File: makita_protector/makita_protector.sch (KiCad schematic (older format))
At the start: 42 parts, among them J1 Jack-DC, Q1 SQJ457EP, Q2 BSS123, SW1 FORCE_ON, SW2 FORCE_OFF, U1 TPS54302, U2 LM2903

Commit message: first layout
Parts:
- removed C1, C12: 100n, symbol Device:C
- removed C2, C4, C7, C9: 10u, symbol Device:C
- removed C6: 100p, symbol Device:C
- removed J1: Jack-DC, symbol Connector:Jack-DC
- removed L1: INDUCTOR, symbol pspice:INDUCTOR
- removed R1, R2: R, symbol Device:R
- removed R5: 47R, symbol Device:R
- removed R6: 100k, symbol Device:R
- removed R7: 5k6, symbol Device:R
- removed SW1: FORCE_ON, symbol Switch:SW_Push
- removed SW2: FORCE_OFF, symbol Switch:SW_Push
- removed U1: TPS54302, Package_TO_SOT_SMD:SOT-23-6, symbol Regulator_Switching:TPS54302
- added F2: Fuse, Fuse:Fuse_0603_1608Metric, symbol Device:Fuse
- added H? (x4): MountingHole, symbol Mechanical:MountingHole
- added J1: 12V, TestPoint:TestPoint_Plated_Hole_D2.0mm, symbol Connector_Generic:Conn_01x01
- added J2, J4, J6: GND, TestPoint:TestPoint_Plated_Hole_D2.0mm, symbol Connector_Generic:Conn_01x01
- added J3: FORCE_ON, TestPoint:TestPoint_Plated_Hole_D2.0mm, symbol Connector_Generic:Conn_01x01
- added J5: FORCE_OFF, TestPoint:TestPoint_Plated_Hole_D2.0mm, symbol Connector_Generic:Conn_01x01
- BT1: footprint (none) -> makita_protector:contact_plates
- C10, C3, C5, C8: footprint (none) -> Capacitor_SMD:C_0805_2012Metric
- C13: renamed from C11; footprint (none) -> Capacitor_SMD:C_0805_2012Metric
- F1: footprint (none) -> Fuse:Fuse_1206_3216Metric
- R10: renamed from R12; footprint (none) -> Resistor_SMD:R_0805_2012Metric
- R13: renamed from R10; footprint (none) -> Resistor_SMD:R_0805_2012Metric
- R14: renamed from R11; footprint (none) -> Resistor_SMD:R_0805_2012Metric
- R15: renamed from R13; footprint (none) -> Resistor_SMD:R_0805_2012Metric
- R16: renamed from R14; footprint (none) -> Resistor_SMD:R_0805_2012Metric
- R20: renamed from R15; footprint (none) -> Resistor_SMD:R_0805_2012Metric
- R21: renamed from R16; footprint (none) -> Resistor_SMD:R_0805_2012Metric
- R3, R4, R8, R9: footprint (none) -> Resistor_SMD:R_0805_2012Metric
- U2: footprint (none) -> Package_SO:SOIC-8_3.9x4.9mm_P1.27mm
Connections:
- net +12V: now also J1.1 (Pin_1)
- net +BATT: now also F2.1
- net GND: now also J2.1 (Pin_1), J4.1 (Pin_1), J6.1 (Pin_1)
- net at BT1.1 (+), F1.2: now also F2.2
- net at C3.2: now also J3.1 (Pin_1)
- net at R16.2: now also J5.1 (Pin_1)
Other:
- note removed: "DCDC"
- note removed: "EN pin maximum 6V!"
- note removed: "battery voltage to output voltage"
- moved on the sheet: BT1, C10, C13, C3, C5, C8, D1, D2, D3, D4, F1, Q1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

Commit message: updated layput
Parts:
- H1, H2, H3, H4: renamed from H?; footprint (none) -> MountingHole:MountingHole_3.2mm_M3_DIN965
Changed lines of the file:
@@
 F 0 "#LOGO1" H 6000 7375 50  0001 C CNN
 F 1 "Logo_Open_Hardware_Small" H 6000 6875 50  0001 C CNN
-F 2 "" H 6000 7100 50  0001 C CNN
+F 2 "Symbol:OSHW-Logo2_9.8x8mm_Copper" H 6000 7100 50  0001 C CNN
 F 3 "~" H 6000 7100 50  0001 C CNN
 	1    6000 7100
@@
 	9600 1950 9600 2700
 $Comp
-L Mechanical:MountingHole H?
+L Mechanical:MountingHole H1
 U 1 1 6025B2E9
 P 1000 6400
-F 0 "H?" H 1100 6446 50  0000 L CNN
+F 0 "H1" H 1100 6446 50  0000 L CNN
 F 1 "MountingHole" H 1100 6355 50  0000 L CNN
-F 2 "" H 1000 6400 50  0001 C CNN
+F 2 "MountingHole:MountingHole_3.2mm_M3_DIN965" H 1000 6400 50  0001 C CNN
 F 3 "~" H 1000 6400 50  0001 C CNN
 	1    1000 6400
@@
 $EndComp
 $Comp
-L Mechanical:MountingHole H?
+L Mechanical:MountingHole H2
 U 1 1 6025BA60
 P 1000 6600
-F 0 "H?" H 1100 6646 50  0000 L CNN
+F 0 "H2" H 1100 6646 50  0000 L CNN
 F 1 "MountingHole" H 1100 6555 50  0000 L CNN
-F 2 "" H 1000 6600 50  0001 C CNN
+F 2 "MountingHole:MountingHole_3.2mm_M3_DIN965" H 1000 6600 50  0001 C CNN
 F 3 "~" H 1000 6600 50  0001 C CNN
 	1    1000 6600
@@
 $EndComp
 $Comp
-L Mechanical:MountingHole H?
+L Mechanical:MountingHole H3
 U 1 1 6025C1C4
 P 1000 6800
-F 0 "H?" H 1100 6846 50  0000 L CNN
+F 0 "H3" H 1100 6846 50  0000 L CNN
 F 1 "MountingHole" H 1100 6755 50  0000 L CNN
-F 2 "" H 1000 6800 50  0001 C CNN
+F 2 "MountingHole:MountingHole_3.2mm_M3_DIN965" H 1000 6800 50  0001 C CNN
 F 3 "~" H 1000 6800 50  0001 C CNN
 	1    1000 6800
@@
 $EndComp
 $Comp
-L Mechanical:MountingHole H?
+L Mechanical:MountingHole H4
 U 1 1 6025C1CA
 P 1000 7000
-F 0 "H?" H 1100 7046 50  0000 L CNN
+F 0 "H4" H 1100 7046 50  0000 L CNN
 F 1 "MountingHole" H 1100 6955 50  0000 L CNN
-F 2 "" H 1000 7000 50  0001 C CNN
+F 2 "MountingHole:MountingHole_3.2mm_M3_DIN965" H 1000 7000 50  0001 C CNN
 F 3 "~" H 1000 7000 50  0001 C CNN
 	1    1000 7000
 	1    0    0    -1
 $EndComp
+$Comp
+L Graphic:Logo_Open_Hardware_Small #LOGO2
+U 1 1 6004B459
+P 4950 7100
+F 0 "#LOGO2" H 4950 7375 50  0001 C CNN
+F 1 "Kicad" H 4950 6875 50  0000 C CNN
+F 2 "Symbol:KiCad-Logo2_8mm_Copper" H 4950 7100 50  0001 C CNN
+F 3 "~" H 4950 7100 50  0001 C CNN
+	1    4950 7100
+	1    0    0    -1
+$EndComp

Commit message: final version for production v1
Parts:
- added FID1, FID2, FID3: Fiducial, makita_protector:Fiducial_1mm_Mask2mm_Paste, symbol Mechanical:Fiducial
- added LOGO1: oshw, Symbol:OSHW-Logo2_7.3x6mm_SilkScreen, symbol Graphic:Logo_Open_Hardware_Small
- added LOGO2: Kicad, Symbol:KiCad-Logo2_5mm_SilkScreen, symbol Graphic:Logo_Open_Hardware_Small
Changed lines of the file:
@@
 Connection ~ 1500 1400
 $Comp
-L Graphic:Logo_Open_Hardware_Small #LOGO1
+L Graphic:Logo_Open_Hardware_Small LOGO1
 U 1 1 6012B83E
 P 6000 7100
-F 0 "#LOGO1" H 6000 7375 50  0001 C CNN
-F 1 "Logo_Open_Hardware_Small" H 6000 6875 50  0001 C CNN
-F 2 "Symbol:OSHW-Logo2_9.8x8mm_Copper" H 6000 7100 50  0001 C CNN
+F 0 "LOGO1" H 6000 7375 50  0001 C CNN
+F 1 "oshw" H 6000 6875 50  0000 C CNN
+F 2 "Symbol:OSHW-Logo2_7.3x6mm_SilkScreen" H 6000 7100 50  0001 C CNN
 F 3 "~" H 6000 7100 50  0001 C CNN
 	1    6000 7100
@@
 $EndComp
 $Comp
-L Graphic:Logo_Open_Hardware_Small #LOGO2
+L Graphic:Logo_Open_Hardware_Small LOGO2
 U 1 1 6004B459
 P 4950 7100
-F 0 "#LOGO2" H 4950 7375 50  0001 C CNN
+F 0 "LOGO2" H 4950 7375 50  0001 C CNN
 F 1 "Kicad" H 4950 6875 50  0000 C CNN
-F 2 "Symbol:KiCad-Logo2_8mm_Copper" H 4950 7100 50  0001 C CNN
+F 2 "Symbol:KiCad-Logo2_5mm_SilkScreen" H 4950 7100 50  0001 C CNN
 F 3 "~" H 4950 7100 50  0001 C CNN
 	1    4950 7100
 	1    0    0    -1
 $EndComp
+$Comp
+L Mechanical:Fiducial FID1
+U 1 1 60086B21
+P 2350 6400
+F 0 "FID1" H 2435 6446 50  0000 L CNN
+F 1 "Fiducial" H 2435 6355 50  0000 L CNN
+F 2 "makita_protector:Fiducial_1mm_Mask2mm_Paste" H 2350 6400 50  0001 C CNN
+F 3 "~" H 2350 6400 50  0001 C CNN
+	1    2350 6400
+	1    0    0    -1
+$EndComp
+$Comp
+L Mechanical:Fiducial FID2
+U 1 1 60087198
+P 2350 6650
+F 0 "FID2" H 2435 6696 50  0000 L CNN
+F 1 "Fiducial" H 2435 6605 50  0000 L CNN
+F 2 "makita_protector:Fiducial_1mm_Mask2mm_Paste" H 2350 6650 50  0001 C CNN
+F 3 "~" H 2350 6650 50  0001 C CNN
+	1    2350 6650
+	1    0    0    -1
+$EndComp
+$Comp
+L Mechanical:Fiducial FID3
+U 1 1 60087324
+P 2350 6900
+F 0 "FID3" H 2435 6946 50  0000 L CNN
+F 1 "Fiducial" H 2435 6855 50  0000 L CNN
+F 2 "makita_protector:Fiducial_1mm_Mask2mm_Paste" H 2350 6900 50  0001 C CNN
+F 3 "~" H 2350 6900 50  0001 C CNN
+	1    2350 6900
+	1    0    0    -1
+$EndComp

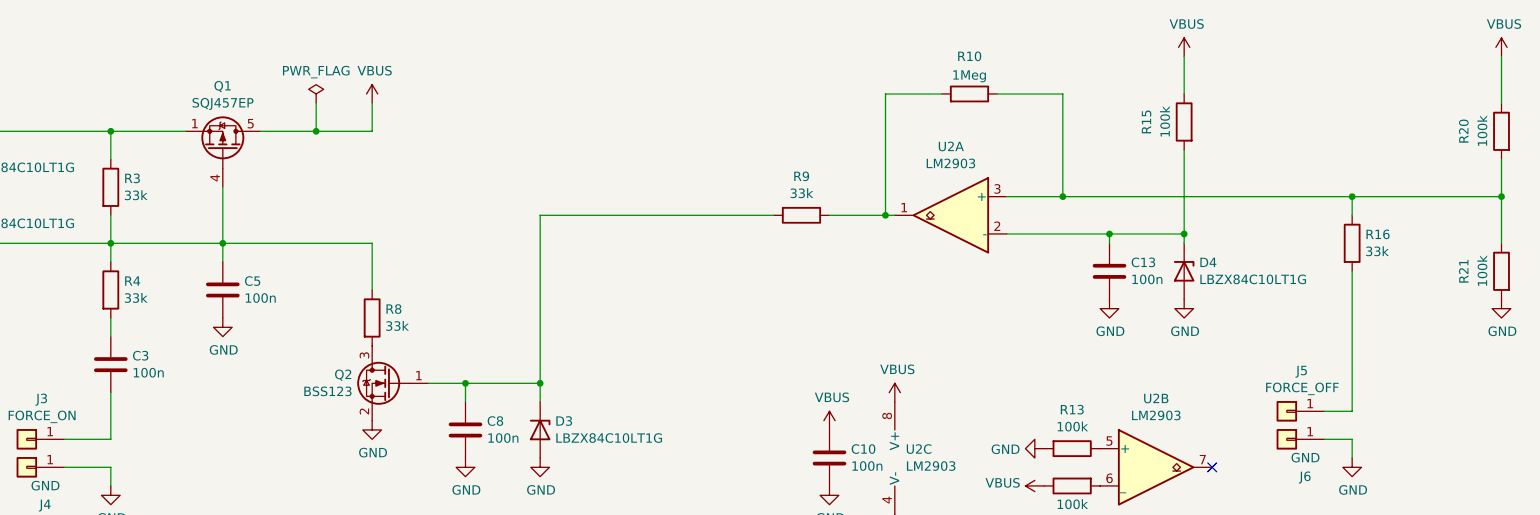
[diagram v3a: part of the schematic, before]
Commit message: updated values after initial testing
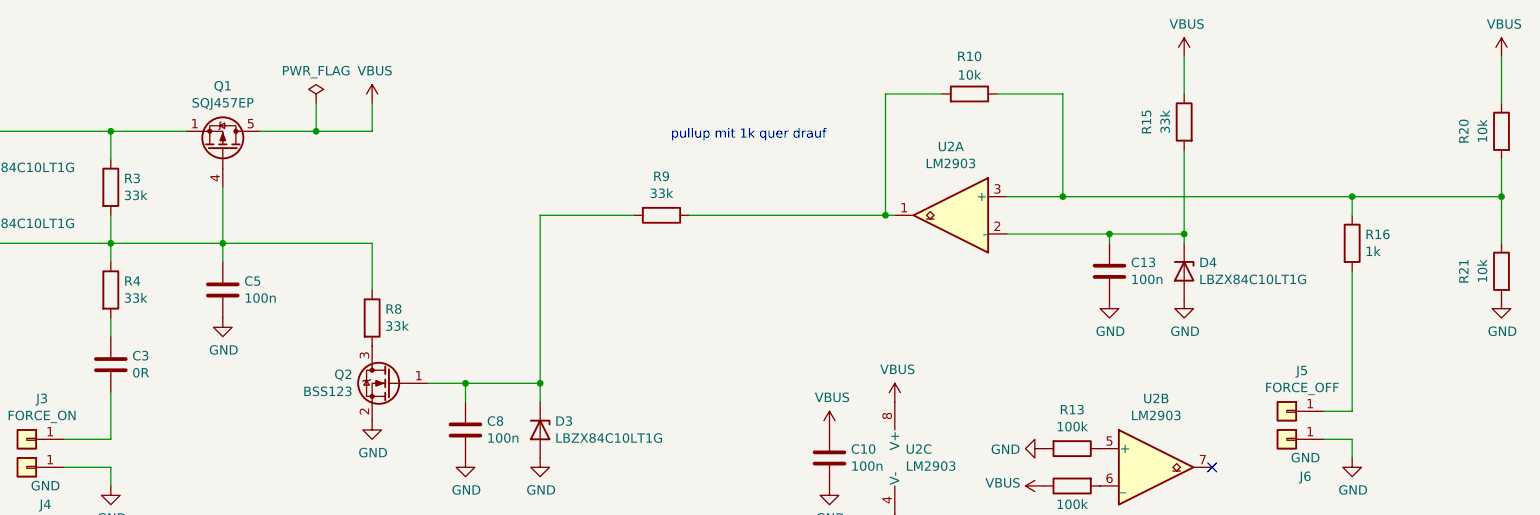
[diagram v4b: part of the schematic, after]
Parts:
- C3: value 100n -> 0R
- R10: value 1Meg -> 10k
- R15: value 100k -> 33k
- R16: value 33k -> 1k
- R20, R21: value 100k -> 10k
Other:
- note added: "pullup mit 1k quer drauf"
- moved on the sheet: R9
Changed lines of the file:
@@
 L Device:R R9
 U 1 1 6001C131
-P 6650 1650
-F 0 "R9" V 6443 1650 50  0000 C CNN
-F 1 "33k" V 6534 1650 50  0000 C CNN
-F 2 "Resistor_SMD:R_0805_2012Metric" V 6580 1650 50  0001 C CNN
-F 3 "~" H 6650 1650 50  0001 C CNN
-	1    6650 1650
+P 5900 1650
+F 0 "R9" V 5693 1650 50  0000 C CNN
+F 1 "33k" V 5784 1650 50  0000 C CNN
+F 2 "Resistor_SMD:R_0805_2012Metric" V 5830 1650 50  0001 C CNN
+F 3 "~" H 5900 1650 50  0001 C CNN
+	1    5900 1650
 	0    1    1    0
 $EndComp
@@
 P 8700 1150
 F 0 "R15" V 8900 1150 50  0000 C CNN
-F 1 "100k" V 8800 1150 50  0000 C CNN
+F 1 "33k" V 8800 1150 50  0000 C CNN
 F 2 "Resistor_SMD:R_0805_2012Metric" V 8630 1150 50  0001 C CNN
 F 3 "~" H 8700 1150 50  0001 C CNN
@@
 P 10400 1950
 F 0 "R21" V 10600 1950 50  0000 C CNN
-F 1 "100k" V 10500 1950 50  0000 C CNN
+F 1 "10k" V 10500 1950 50  0000 C CNN
 F 2 "Resistor_SMD:R_0805_2012Metric" V 10330 1950 50  0001 C CNN
 F 3 "~" H 10400 1950 50  0001 C CNN
@@
 P 10400 1200
 F 0 "R20" V 10600 1200 50  0000 C CNN
-F 1 "100k" V 10500 1200 50  0000 C CNN
+F 1 "10k" V 10500 1200 50  0000 C CNN
 F 2 "Resistor_SMD:R_0805_2012Metric" V 10330 1200 50  0001 C CNN
 F 3 "~" H 10400 1200 50  0001 C CNN
@@
 P 7550 1000
 F 0 "R10" V 7750 1000 50  0000 C CNN
-F 1 "1Meg" V 7650 1000 50  0000 C CNN
+F 1 "10k" V 7650 1000 50  0000 C CNN
 F 2 "Resistor_SMD:R_0805_2012Metric" V 7480 1000 50  0001 C CNN
 F 3 "~" H 7550 1000 50  0001 C CNN
@@
 Connection ~ 7100 1650
 Wire Wire Line
-	7100 1650 6800 1650
+	7100 1650 6050 1650
 $Comp
 L Device:R R4
@@
 P 2950 2450
 F 0 "C3" H 3065 2496 50  0000 L CNN
-F 1 "100n" H 3065 2405 50  0000 L CNN
+F 1 "0R" H 3065 2405 50  0000 L CNN
 F 2 "Capacitor_SMD:C_0805_2012Metric" H 2988 2300 50  0001 C CNN
 F 3 "~" H 2950 2450 50  0001 C CNN
@@
 P 9600 1800
 F 0 "R16" H 9670 1846 50  0000 L CNN
-F 1 "33k" H 9670 1755 50  0000 L CNN
+F 1 "1k" H 9670 1755 50  0000 L CNN
 F 2 "Resistor_SMD:R_0805_2012Metric" V 9530 1800 50  0001 C CNN
 F 3 "~" H 9600 1800 50  0001 C CNN
@@
 	5250 2550 5250 1650
 Wire Wire Line
-	5250 1650 6500 1650
+	5250 1650 5750 1650
 Connection ~ 5250 2550
 $Comp
@@
 	1    0    0    -1
 $EndComp
+Text Notes 5950 1250 0    50   ~ 0
+pullup mit 1k quer drauf
 $EndSCHEMATC
